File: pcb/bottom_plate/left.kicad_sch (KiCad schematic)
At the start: 15 parts

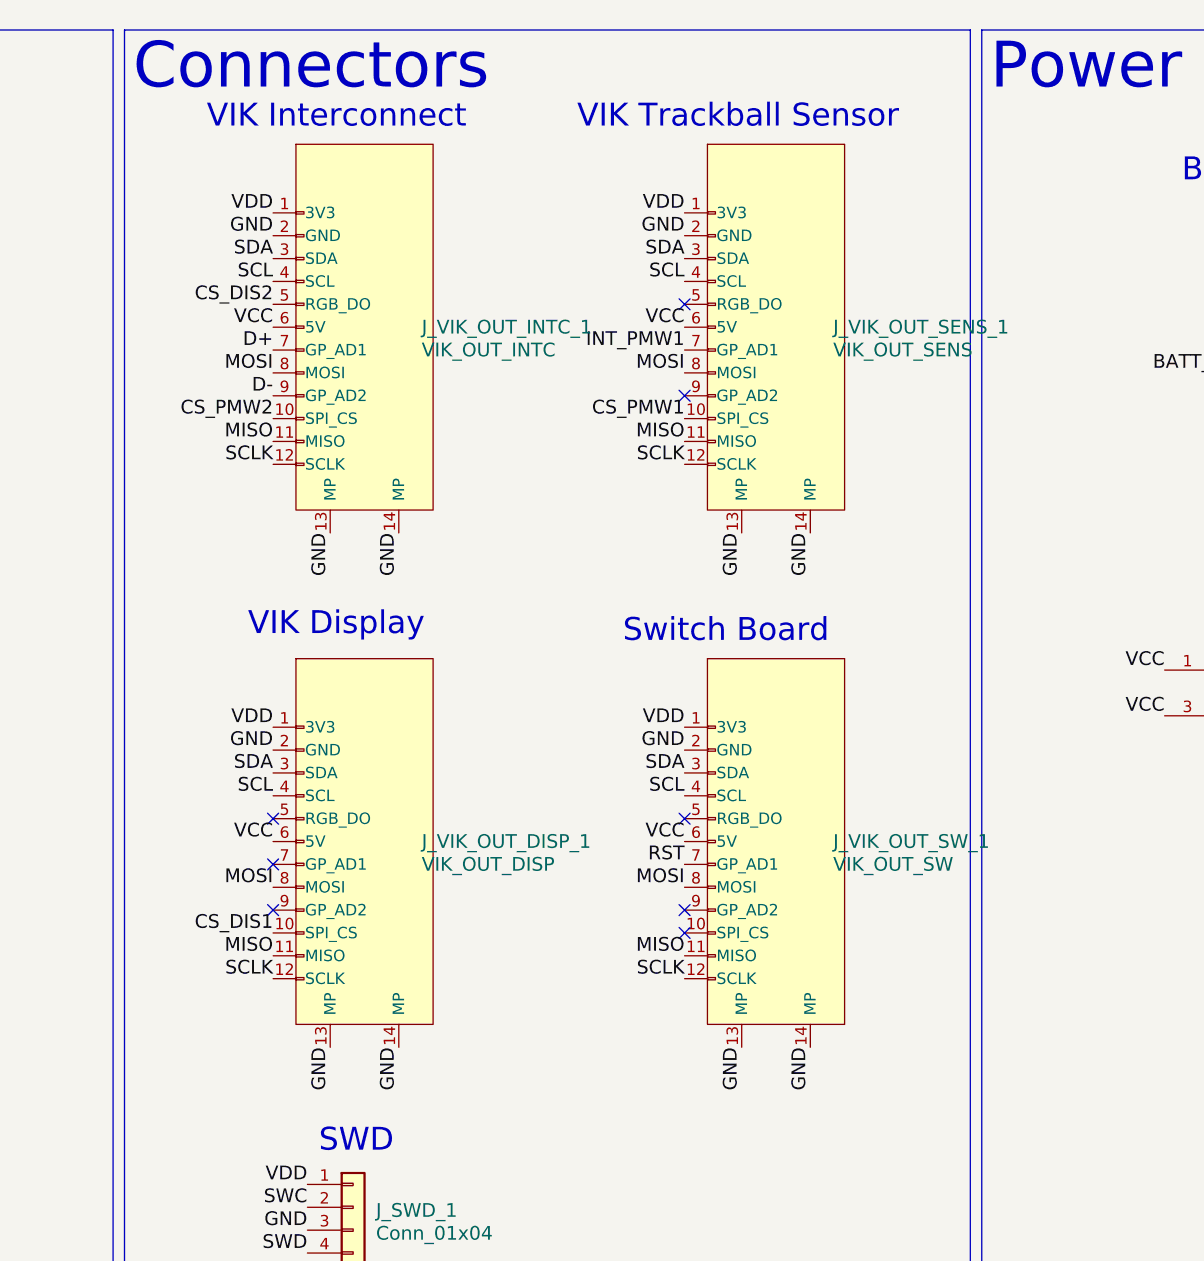
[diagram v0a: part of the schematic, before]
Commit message: Update KiCAD projects to use new library locations.
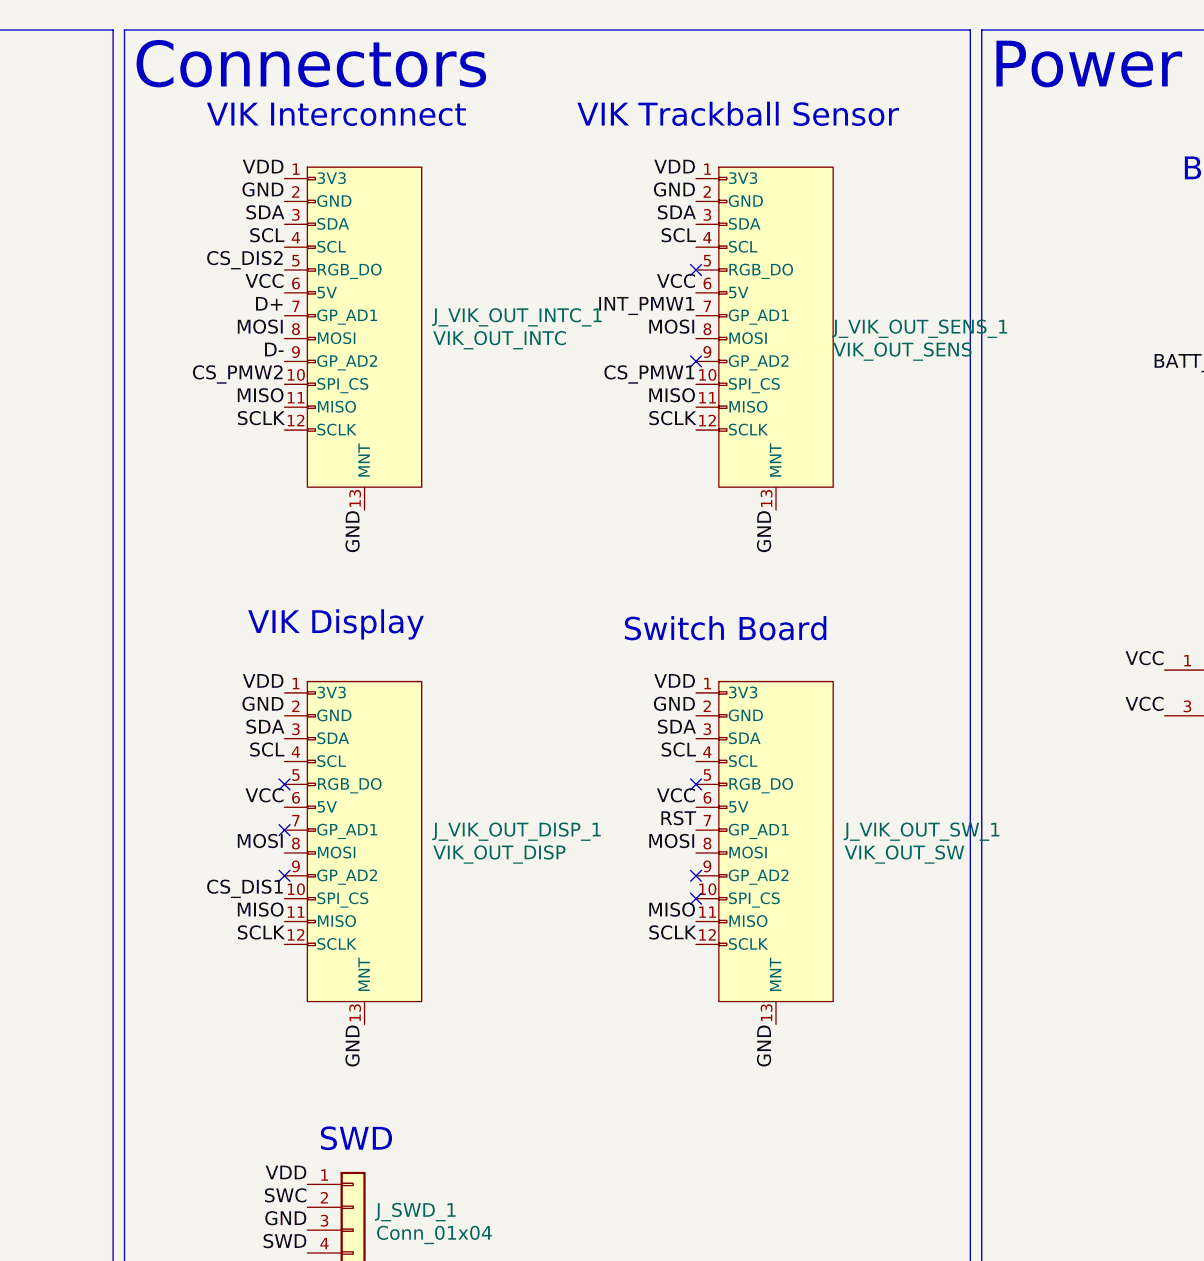
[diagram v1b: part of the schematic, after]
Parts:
- J_VIK_OUT_DISP_1, J_VIK_OUT_INTC_1, J_VIK_OUT_SENS_1, J_VIK_OUT_SW_1: footprint vik:vik-keyboard-connector-horizontal -> footprints:vik-keyboard-connector-horizontal
- U_MCU_1: footprint mcu:holyiot-18010-no-underside -> footprints:holyiot-18010-no-underside
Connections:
- net GND: no longer J_VIK_OUT_DISP_1.14 (MP), J_VIK_OUT_INTC_1.14 (MP), J_VIK_OUT_SENS_1.14 (MP), J_VIK_OUT_SW_1.14 (MP)
